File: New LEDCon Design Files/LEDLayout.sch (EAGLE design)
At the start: 16 parts

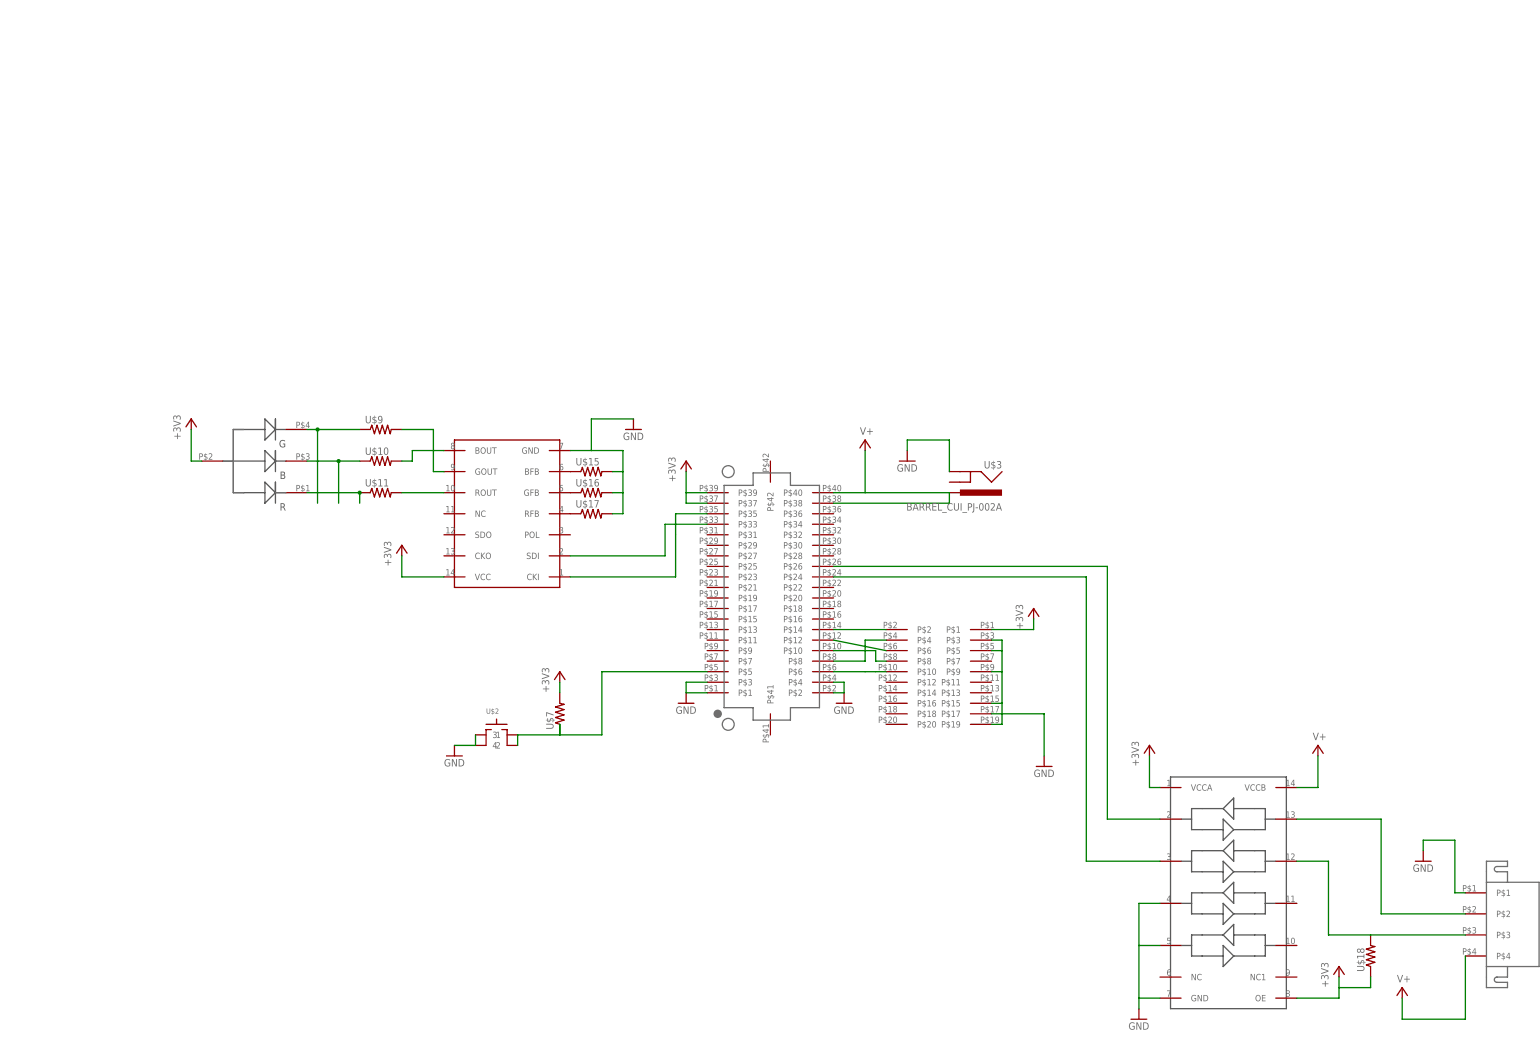
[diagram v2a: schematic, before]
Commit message: Prototype 3
Added filter caps and output data /clk pullups
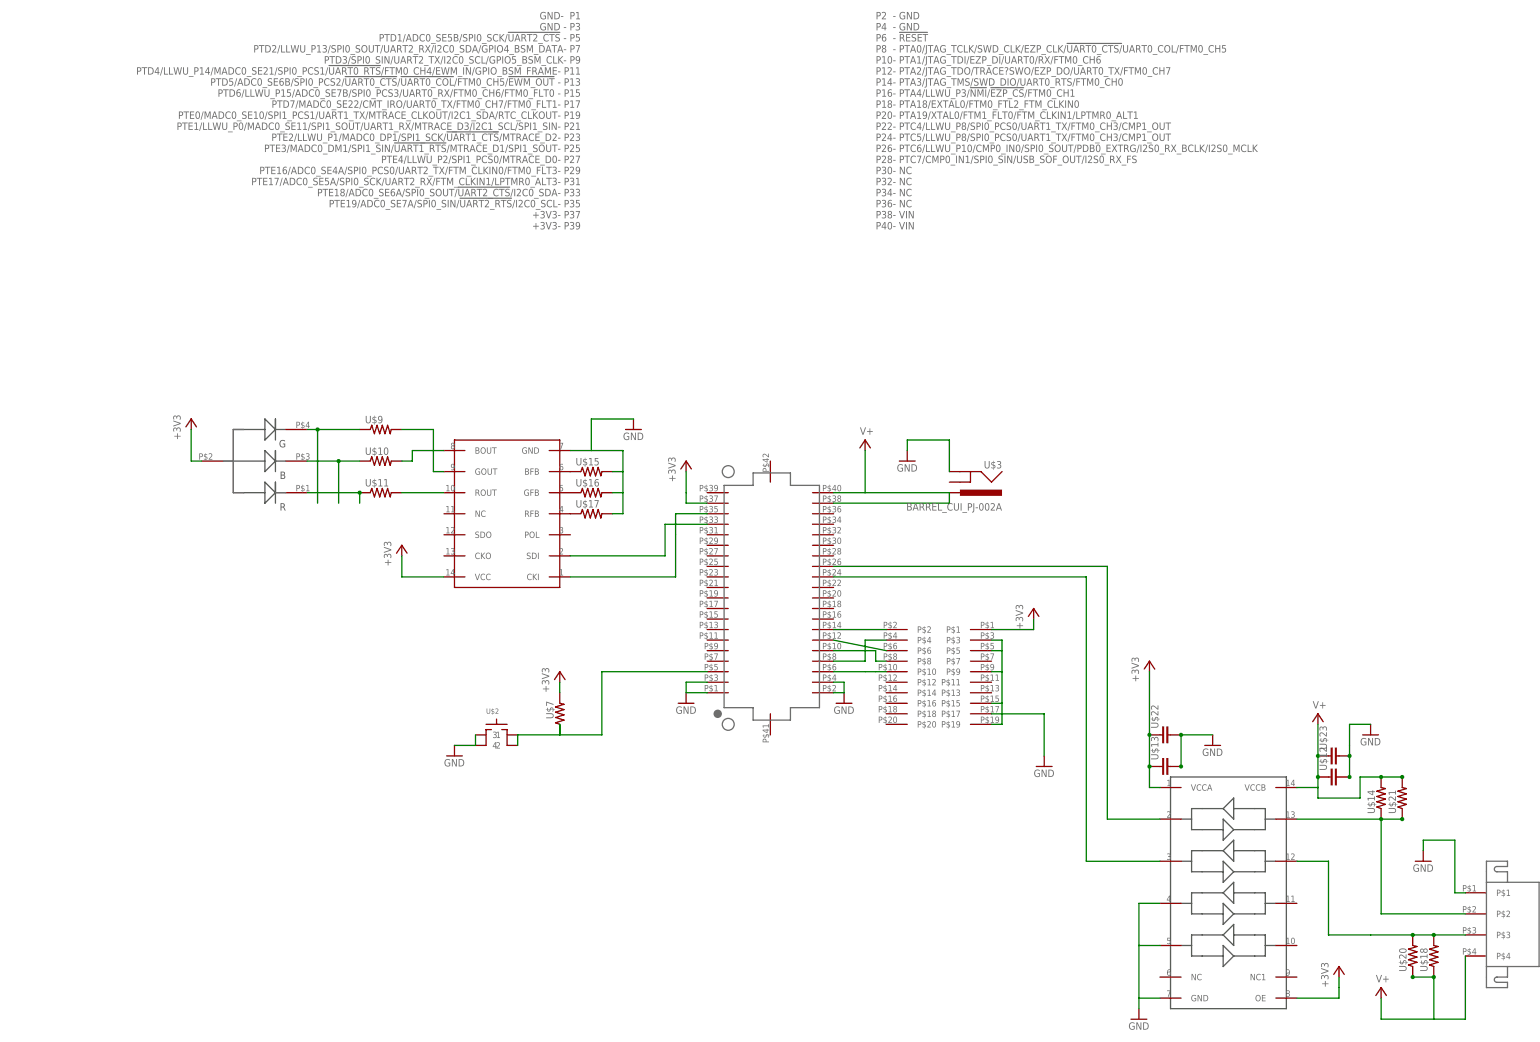
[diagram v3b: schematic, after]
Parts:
- added U$12, U$13: (no value), GW-devices:RF-C0402
- added U$14: (no value), GW-devices:RF-R0402
- added U$20, U$21: (no value), GW-devices:RF-R0805
- added U$22, U$23: (no value), GW-devices:RF-C0805
- U$18: device GW-devices:RF-R0805 -> GW-devices:RF-R0402
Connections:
- net +3V3: now also U$13.1, U$22.1, U$4.+3V3@1; no longer U$18.1, U$4.P$37, U$4.P$39
- net CLK_5V: now also U$20.2
- net DAT_5V: now also U$14.1, U$21.1
- net GND: now also U$12.2, U$13.2, U$22.2, U$23.2, U$4.GND@1, U$4.GND@2, U$4.GND@3, U$4.GND@4; no longer U$4.P$1, U$4.P$2, U$4.P$3, U$4.P$4
- net N$1: now also U$4.PTC6/LLWU_P10/CMP0_IN0/SPI0_SOUT/PDB0_EXTRG/I2S0_RX_BCLK/I2S0_MCLK; no longer U$4.P$26
- net N$10: now also U$4.PTE18/ADC0_SE6A/SPI0_SOUT/!UART2_CTS!/I2C0_SDA; no longer U$4.P$33
- net N$14: now also U$4.PTE19/ADC0_SE7A/SPI0_SIN/!UART2_RTS!/I2C0_SCL; no longer U$4.P$35
- net N$18: now also U$4.PTA0/JTAG_TCLK/SWD_CLK/EZP_CLK/!UART0_CTS/!UART0_COL/FTM0_CH5; no longer U$4.P$8
- net N$19: now also U$4.PTA3/JTAG_TMS/SWD_DIO/UART0_RTS/FTM0_CH0; no longer U$4.P$14
- net N$2: now also U$4.PTC5/LLWU_P8/SPI0_PCS0/UART1_TX/FTM0_CH3/CMP1_OUT; no longer U$4.P$24
- net N$20: now also U$4.PTA1/JTAG_TDI/EZP_DI/UART0/RX/FTM0_CH6; no longer U$4.P$10
- net N$21: now also U$4.!RESET; no longer U$4.P$6
- net N$22: now also U$4.PTA2/JTAG_TDO/TRACE?SWO/EZP_DO/UART0_TX/FTM0_CH7; no longer U$4.P$12
- net N$3: now also U$4.PTD1/ADC0_SE5B/SPI0_SCK/!UART2_CTS; no longer U$4.P$5
- net V+: now also U$12.1, U$14.2, U$18.1, U$20.1, U$21.2, U$23.1, U$4.VIN@1, U$4.VIN@2; no longer U$4.P$38, U$4.P$40
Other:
- moved on the sheet: U$18
